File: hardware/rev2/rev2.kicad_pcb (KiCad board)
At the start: 4 copper layers, 60 x 40 mm, 1 part, among them U1 SX1262IMLTRT

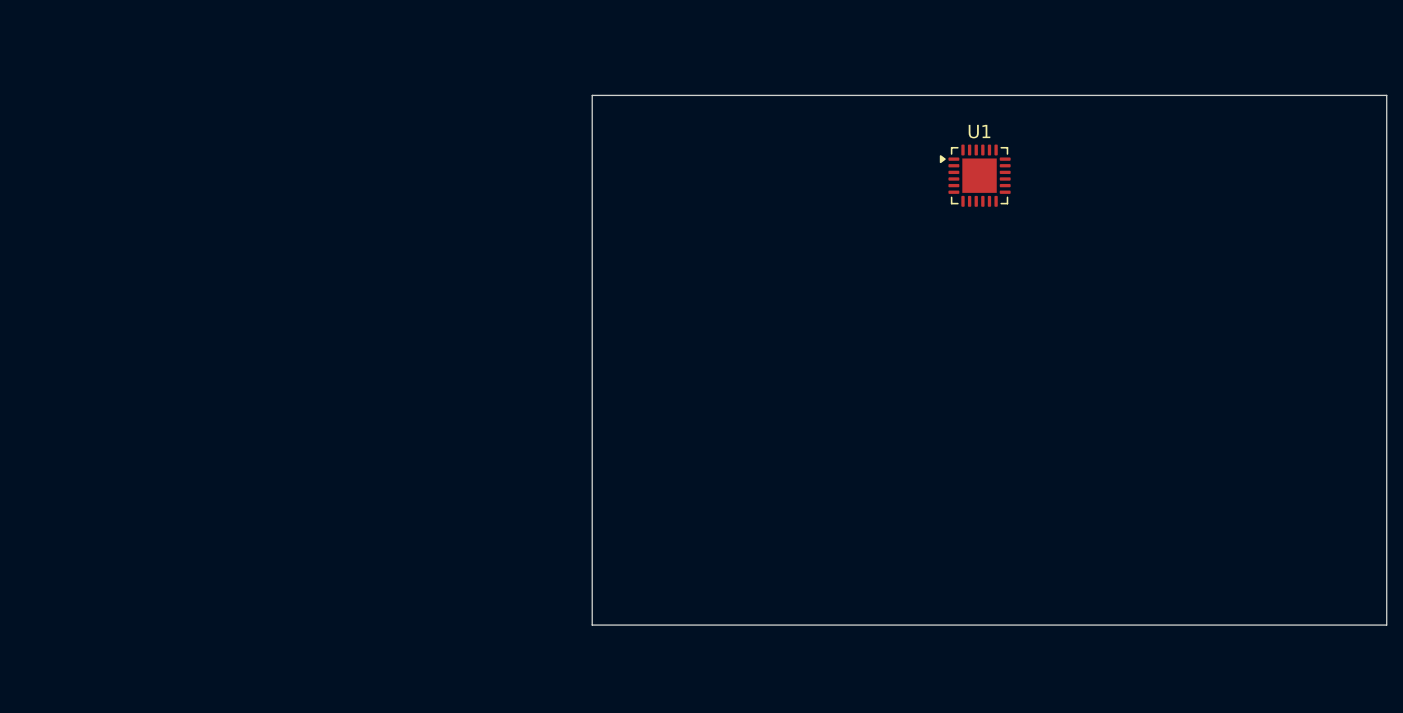
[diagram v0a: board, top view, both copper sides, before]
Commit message: fixed some ERC errors and warnings, added USB, assigned a bunch of footprints
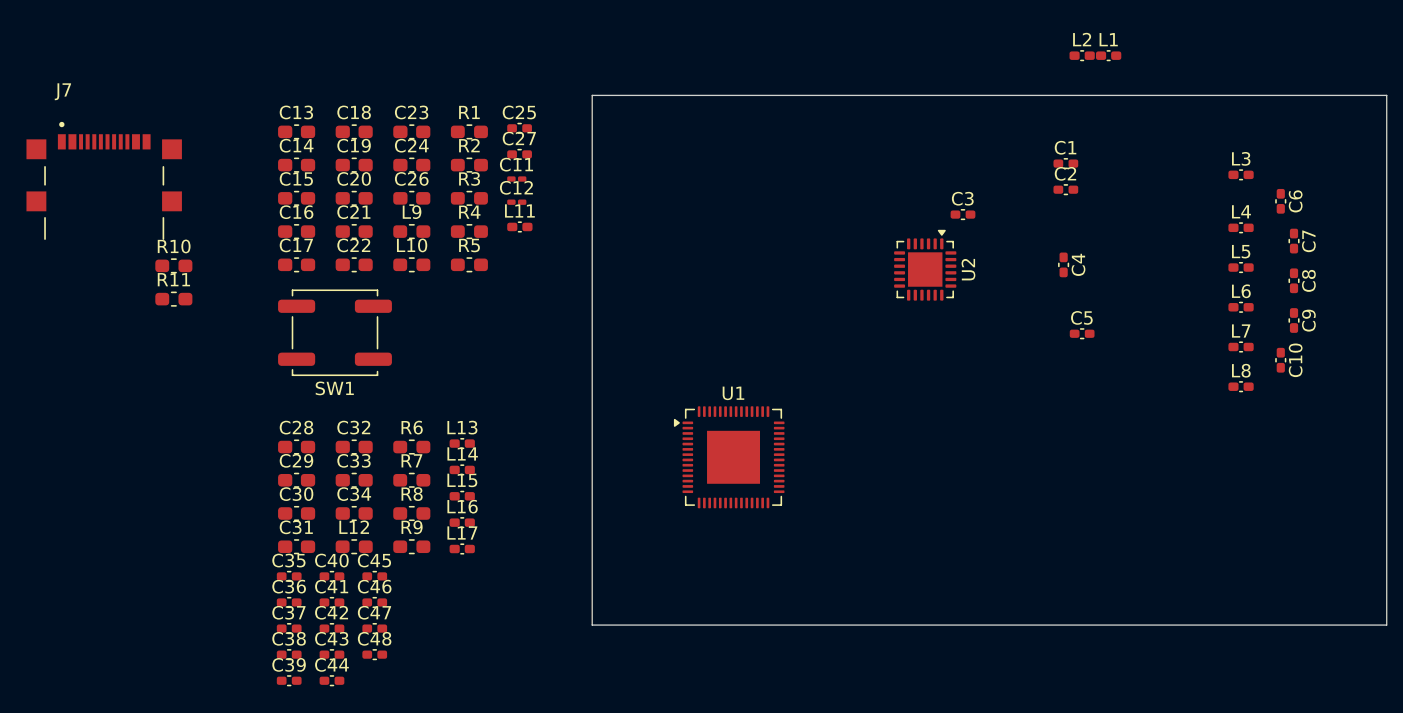
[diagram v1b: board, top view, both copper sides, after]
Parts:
- added C1: TBD, Capacitor_SMD:C_0402_1005Metric_Pad0.74x0.62mm_HandSolder, F.Cu at (163.8, 62.1)
- added C10: DC-Block, Capacitor_SMD:C_0402_1005Metric_Pad0.74x0.62mm_HandSolder, F.Cu at (180.0, 77.0)
- added C11: NC, Capacitor_SMD:C_0201_0603Metric_Pad0.64x0.40mm_HandSolder, F.Cu at (122.3, 63.3)
- added C12: NC, Capacitor_SMD:C_0201_0603Metric_Pad0.64x0.40mm_HandSolder, F.Cu at (122.3, 65.1)
- added C13: 10 uF, Capacitor_SMD:C_0603_1608Metric_Pad1.08x0.95mm_HandSolder, F.Cu at (105.7, 59.8)
- added C14: TBD, Capacitor_SMD:C_0603_1608Metric_Pad1.08x0.95mm_HandSolder, F.Cu at (105.7, 62.3)
- added C15: 1 uF, Capacitor_SMD:C_0603_1608Metric_Pad1.08x0.95mm_HandSolder, F.Cu at (105.7, 64.8)
- added C16: 0.1 uF, Capacitor_SMD:C_0603_1608Metric_Pad1.08x0.95mm_HandSolder, F.Cu at (105.7, 67.3)
- added C17: 1 uF, Capacitor_SMD:C_0603_1608Metric_Pad1.08x0.95mm_HandSolder, F.Cu at (105.7, 69.8)
- added C18: TBD, Capacitor_SMD:C_0603_1608Metric_Pad1.08x0.95mm_HandSolder, F.Cu at (110.0, 59.8)
- added C19: 0.1 uF, Capacitor_SMD:C_0603_1608Metric_Pad1.08x0.95mm_HandSolder, F.Cu at (110.0, 62.3)
- added C2: TBD, Capacitor_SMD:C_0402_1005Metric_Pad0.74x0.62mm_HandSolder, F.Cu at (163.8, 64.1)
- added C20: 0.1 uF, Capacitor_SMD:C_0603_1608Metric_Pad1.08x0.95mm_HandSolder, F.Cu at (110.0, 64.8)
- added C21: 10 nF, Capacitor_SMD:C_0603_1608Metric_Pad1.08x0.95mm_HandSolder, F.Cu at (110.0, 67.3)
- added C22: 0.1 uF, Capacitor_SMD:C_0603_1608Metric_Pad1.08x0.95mm_HandSolder, F.Cu at (110.0, 69.8)
- added C23: 0.1 uF, Capacitor_SMD:C_0603_1608Metric_Pad1.08x0.95mm_HandSolder, F.Cu at (114.4, 59.8)
- added C24: 1 uF, Capacitor_SMD:C_0603_1608Metric_Pad1.08x0.95mm_HandSolder, F.Cu at (114.4, 62.3)
- added C25: TBD, Capacitor_SMD:C_0402_1005Metric_Pad0.74x0.62mm_HandSolder, F.Cu at (122.5, 59.5)
- added C26: 1 uF, Capacitor_SMD:C_0603_1608Metric_Pad1.08x0.95mm_HandSolder, F.Cu at (114.4, 64.8)
- added C27: TBD, Capacitor_SMD:C_0402_1005Metric_Pad0.74x0.62mm_HandSolder, F.Cu at (122.5, 61.5)
- added C28: 100n, Capacitor_SMD:C_0603_1608Metric_Pad1.08x0.95mm_HandSolder, F.Cu at (105.7, 83.6)
- added C29: TBD, Capacitor_SMD:C_0603_1608Metric_Pad1.08x0.95mm_HandSolder, F.Cu at (105.7, 86.1)
- added C3: TBD, Capacitor_SMD:C_0402_1005Metric_Pad0.74x0.62mm_HandSolder, F.Cu at (156.0, 66.0)
- added C30: 10p, Capacitor_SMD:C_0603_1608Metric_Pad1.08x0.95mm_HandSolder, F.Cu at (105.7, 88.6)
- added C31: 100n, Capacitor_SMD:C_0603_1608Metric_Pad1.08x0.95mm_HandSolder, F.Cu at (105.7, 91.1)
- added C32: 100n, Capacitor_SMD:C_0603_1608Metric_Pad1.08x0.95mm_HandSolder, F.Cu at (110.0, 83.6)
- added C33: TBD, Capacitor_SMD:C_0603_1608Metric_Pad1.08x0.95mm_HandSolder, F.Cu at (110.0, 86.1)
- added C34: 470n, Capacitor_SMD:C_0603_1608Metric_Pad1.08x0.95mm_HandSolder, F.Cu at (110.0, 88.6)
- added C35: DC Block, Capacitor_SMD:C_0402_1005Metric_Pad0.74x0.62mm_HandSolder, F.Cu at (105.1, 93.3)
- added C36: C, Capacitor_SMD:C_0402_1005Metric_Pad0.74x0.62mm_HandSolder, F.Cu at (105.1, 95.3)
- added C37: 47p, Capacitor_SMD:C_0402_1005Metric_Pad0.74x0.62mm_HandSolder, F.Cu at (105.1, 97.3)
- added C38: 47n, Capacitor_SMD:C_0402_1005Metric_Pad0.74x0.62mm_HandSolder, F.Cu at (105.1, 99.2)
- added C39: C, Capacitor_SMD:C_0402_1005Metric_Pad0.74x0.62mm_HandSolder, F.Cu at (105.1, 101.2)
- added C4: TBD, Capacitor_SMD:C_0402_1005Metric_Pad0.74x0.62mm_HandSolder, F.Cu at (163.6, 69.8)
- added C40: C, Capacitor_SMD:C_0402_1005Metric_Pad0.74x0.62mm_HandSolder, F.Cu at (108.3, 93.3)
- added C41: C, Capacitor_SMD:C_0402_1005Metric_Pad0.74x0.62mm_HandSolder, F.Cu at (108.3, 95.3)
- added C42: DC Block, Capacitor_SMD:C_0402_1005Metric_Pad0.74x0.62mm_HandSolder, F.Cu at (108.3, 97.3)
- added C43: C, Capacitor_SMD:C_0402_1005Metric_Pad0.74x0.62mm_HandSolder, F.Cu at (108.3, 99.2)
- added C44: 1n, Capacitor_SMD:C_0402_1005Metric_Pad0.74x0.62mm_HandSolder, F.Cu at (108.3, 101.2)
- added C45: 1n, Capacitor_SMD:C_0402_1005Metric_Pad0.74x0.62mm_HandSolder, F.Cu at (111.6, 93.3)
- added C46: DC Block, Capacitor_SMD:C_0402_1005Metric_Pad0.74x0.62mm_HandSolder, F.Cu at (111.6, 95.3)
- added C47: C, Capacitor_SMD:C_0402_1005Metric_Pad0.74x0.62mm_HandSolder, F.Cu at (111.6, 97.3)
- added C48: C, Capacitor_SMD:C_0402_1005Metric_Pad0.74x0.62mm_HandSolder, F.Cu at (111.6, 99.2)
- added C5: DC-Block, Capacitor_SMD:C_0402_1005Metric_Pad0.74x0.62mm_HandSolder, F.Cu at (165.0, 75.0)
- added C6: DC-Block, Capacitor_SMD:C_0402_1005Metric_Pad0.74x0.62mm_HandSolder, F.Cu at (180.0, 65.0)
- added C7: DC-Block, Capacitor_SMD:C_0402_1005Metric_Pad0.74x0.62mm_HandSolder, F.Cu at (181.0, 68.0)
- added C8: DC-Block, Capacitor_SMD:C_0402_1005Metric_Pad0.74x0.62mm_HandSolder, F.Cu at (181.0, 71.0)
- added C9: DC-Block, Capacitor_SMD:C_0402_1005Metric_Pad0.74x0.62mm_HandSolder, F.Cu at (181.0, 74.0)
- added J7: USB_C_Receptacle_USB2.0_16P, _footprints:SAMESKY_UJ20-C-H-G-SMT-5-P16-TR, F.Cu at (91.1, 64.2)
- added L1: TBD, Inductor_SMD:L_0402_1005Metric_Pad0.77x0.64mm_HandSolder, F.Cu at (167.0, 54.0)
- added L10: 2.0 nH (0.1 nH), Inductor_SMD:L_0603_1608Metric_Pad1.05x0.95mm_HandSolder, F.Cu at (114.4, 69.8)
- added L11: TBD, Inductor_SMD:L_0402_1005Metric_Pad0.77x0.64mm_HandSolder, F.Cu at (122.5, 66.9)
- added L12: 15u, Inductor_SMD:L_0603_1608Metric_Pad1.05x0.95mm_HandSolder, F.Cu at (110.0, 91.1)
- added L13: L, Inductor_SMD:L_0402_1005Metric_Pad0.77x0.64mm_HandSolder, F.Cu at (118.2, 83.3)
- added L14: 115n, Inductor_SMD:L_0402_1005Metric_Pad0.77x0.64mm_HandSolder, F.Cu at (118.2, 85.3)
- added L15: L, Inductor_SMD:L_0402_1005Metric_Pad0.77x0.64mm_HandSolder, F.Cu at (118.2, 87.3)
- added L16: L, Inductor_SMD:L_0402_1005Metric_Pad0.77x0.64mm_HandSolder, F.Cu at (118.2, 89.3)
- added L17: L, Inductor_SMD:L_0402_1005Metric_Pad0.77x0.64mm_HandSolder, F.Cu at (118.2, 91.3)
- added L2: TBD, Inductor_SMD:L_0402_1005Metric_Pad0.77x0.64mm_HandSolder, F.Cu at (165.0, 54.0)
- added L3: Choke, Inductor_SMD:L_0402_1005Metric_Pad0.77x0.64mm_HandSolder, F.Cu at (177.0, 63.0)
- added L4: Choke, Inductor_SMD:L_0402_1005Metric_Pad0.77x0.64mm_HandSolder, F.Cu at (177.0, 67.0)
- added L5: Choke, Inductor_SMD:L_0402_1005Metric_Pad0.77x0.64mm_HandSolder, F.Cu at (177.0, 70.0)
- added L6: Choke, Inductor_SMD:L_0402_1005Metric_Pad0.77x0.64mm_HandSolder, F.Cu at (177.0, 73.0)
- added L7: Choke, Inductor_SMD:L_0402_1005Metric_Pad0.77x0.64mm_HandSolder, F.Cu at (177.0, 76.0)
- added L8: Choke, Inductor_SMD:L_0402_1005Metric_Pad0.77x0.64mm_HandSolder, F.Cu at (177.0, 79.0)
- added L9: TBD (24 nH), Inductor_SMD:L_0603_1608Metric_Pad1.05x0.95mm_HandSolder, F.Cu at (114.4, 67.3)
- added R1: 10K, Inductor_SMD:L_0603_1608Metric_Pad1.05x0.95mm_HandSolder, F.Cu at (118.7, 59.8)
- added R10: 5.1k, Inductor_SMD:L_0603_1608Metric_Pad1.05x0.95mm_HandSolder, F.Cu at (96.4, 69.9)
- added R11: 5.1k, Inductor_SMD:L_0603_1608Metric_Pad1.05x0.95mm_HandSolder, F.Cu at (96.4, 72.4)
- added R2: 22R, Inductor_SMD:L_0603_1608Metric_Pad1.05x0.95mm_HandSolder, F.Cu at (118.7, 62.3)
- added R3: 22R, Inductor_SMD:L_0603_1608Metric_Pad1.05x0.95mm_HandSolder, F.Cu at (118.7, 64.8)
- added R4: 10K, Inductor_SMD:L_0603_1608Metric_Pad1.05x0.95mm_HandSolder, F.Cu at (118.7, 67.3)
- added R5: 10K, Inductor_SMD:L_0603_1608Metric_Pad1.05x0.95mm_HandSolder, F.Cu at (118.7, 69.8)
- added R6: pull-up, Inductor_SMD:L_0603_1608Metric_Pad1.05x0.95mm_HandSolder, F.Cu at (114.4, 83.6)
- added R7: 220R, Inductor_SMD:L_0603_1608Metric_Pad1.05x0.95mm_HandSolder, F.Cu at (114.4, 86.1)
- added R8: 100R, Inductor_SMD:L_0603_1608Metric_Pad1.05x0.95mm_HandSolder, F.Cu at (114.4, 88.6)
- added R9: 100R, Inductor_SMD:L_0603_1608Metric_Pad1.05x0.95mm_HandSolder, F.Cu at (114.4, 91.1)
- added SW1: SW_Push, Button_Switch_SMD:SW_Push_1P1T_NO_CK_KSC7xxJ, F.Cu at (108.6, 74.9)
- added U1: ESP32-S3, Package_DFN_QFN:QFN-56-1EP_7x7mm_P0.4mm_EP4x4mm, F.Cu at (138.7, 84.3)
- moved U2 8.19 mm to (153.2, 70.2), turned to -90 degrees
- renumbered U1 to U2
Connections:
- U2 pad 13: /SX1262/DIO1 -> /ESP32/DIO1
- U2 pad 14: /SX1262/BUSY -> /ESP32/BUSY
- U2 pad 15: /SX1262/RESET -> /SX1262/Reset
- U2 pad 16: /SX1262/MISO -> /ESP32/MISO
- U2 pad 17: /SX1262/MOSI -> /ESP32/MOSI
- U2 pad 18: /SX1262/SCK -> /ESP32/SCK
- U2 pad 19: /SX1262/CS -> /ESP32/CS

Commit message: ESP32 approaching final schematic. tidied up a lot and changed GPIO pins.
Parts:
- L10: value 2.0 nH (0.1 nH) -> 2.0 nH 500mA
- U1: value ESP32-S3 -> ESP32-S3FN8
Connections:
- net /ESP32/XIN renamed Net-(C14-Pad1)
- net /ESP32/XOUT renamed Net-(U1-XTAL_N)
- C13 pad 1: /ESP32/VDD33 -> +3V3
- C15 pad 1: /ESP32/VDD33 -> +3V3
- C16 pad 1: /ESP32/VDD33 -> +3V3
- C17 pad 1: /ESP32/VDD33 -> +3V3
- C19 pad 1: /ESP32/VDD33 -> +3V3
- C21 pad 1: /ESP32/VDD33 -> +3V3
- C22 pad 1: /ESP32/VDD_SPI -> +3V3
- C23 pad 1: /ESP32/VDD33 -> +3V3
- C24 pad 1: /ESP32/VDD_SPI -> +3V3
- L10 pad 1: /ESP32/VDD33 -> +3V3
- R1 pad 1: /ESP32/VDD33 -> +3V3
- R2 pad 2: Net-(U1-GPIO19/USB_D-) -> unconnected-(R2-Pad2)
- R3 pad 1: /USB_D+ -> unconnected-(R3-Pad1)
- R3 pad 2: Net-(U1-GPIO20/USB_D+) -> /USB_D+
- R4 pad 1: +3V3 -> GND
- U1 pad 20: /ESP32/VDD33 -> +3V3
- U1 pad 25: Net-(U1-GPIO19/USB_D-) -> /USB_D-
- U1 pad 26: Net-(U1-GPIO20/USB_D+) -> /USB_D+
- U1 pad 29: /ESP32/VDD_SPI -> +3V3
- U1 pad 46: /ESP32/VDD33 -> +3V3
- U1 pad 55: /ESP32/VDD33 -> +3V3
- U1 pad 56: /ESP32/VDD33 -> +3V3
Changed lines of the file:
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@@
 			(layers "F.Cu" "F.Mask" "F.Paste")
 			(roundrect_rratio 0.25)
-			(net "/ESP32/XIN")
+			(net "Net-(C14-Pad1)")
 			(pintype "passive")
 		)
@@
 			(layers "F.Cu" "F.Mask" "F.Paste")
 			(roundrect_rratio 0.25)
-			(net "/ESP32/VDD33")
+			(net "+3V3")
 			(pintype "passive")
 		)
@@
 			(layers "F.Cu" "F.Mask" "F.Paste")
 			(roundrect_rratio 0.25)
-			(net "Net-(U1-GPIO19{slash}USB_D-)")
+			(net "unconnected-(R2-Pad2)")
 			(pintype "passive")
 		)
@@
 			(layers "F.Cu" "F.Mask" "F.Paste")
 			(roundrect_rratio 0.25)
-			(net "/ESP32/VDD_SPI")
+			(net "+3V3")
 			(pintype "passive")
 		)
@@
 			(layers "F.Cu" "F.Mask" "F.Paste")
 			(roundrect_rratio 0.25)
-			(net "/ESP32/VDD33")
+			(net "+3V3")
 			(pintype "passive")
 		)
@@
 			(layers "F.Cu" "F.Mask" "F.Paste")
 			(roundrect_rratio 0.25)
-			(net "/ESP32/XOUT")
+			(net "Net-(U1-XTAL_N)")
 			(pintype "passive")
 		)
@@
 			)
 		)
-		(property "Value" "ESP32-S3"
+		(property "Value" "ESP32-S3FN8"
 			(at 0 4.8 0)
 			(layer "F.Fab")
@@
 			(layers "F.Cu" "F.Mask" "F.Paste")
 			(roundrect_rratio 0.25)
-			(net "/ESP32/VDD33")
+			(net "+3V3")
 			(pinfunction "VDD3P3_RTC_20")
 			(pintype "power_in")
@@
 			(layers "F.Cu" "F.Mask" "F.Paste")
 			(roundrect_rratio 0.25)
-			(net "Net-(U1-GPIO19{slash}USB_D-)")
+			(net "/USB_D-")
 			(pinfunction "GPIO19/USB_D-_25")
 			(pintype "bidirectional")
@@
 			(layers "F.Cu" "F.Mask" "F.Paste")
 			(roundrect_rratio 0.25)
-			(net "Net-(U1-GPIO20{slash}USB_D+)")
+			(net "/USB_D+")
 			(pinfunction "GPIO20/USB_D+_26")
 			(pintype "bidirectional")
@@
 			(layers "F.Cu" "F.Mask" "F.Paste")
 			(roundrect_rratio 0.25)
-			(net "/ESP32/VDD_SPI")
+			(net "+3V3")
 			(pinfunction "VDD_SPI_29")
 			(pintype "power_in")
@@
 			(layers "F.Cu" "F.Mask" "F.Paste")
 			(roundrect_rratio 0.25)
-			(net "/ESP32/VDD33")
+			(net "+3V3")
 			(pinfunction "VDD3P3_CPU_46")
 			(pintype "power_in")
@@
 			(layers "F.Cu" "F.Mask" "F.Paste")
 			(roundrect_rratio 0.25)
-			(net "/ESP32/XOUT")
+			(net "Net-(U1-XTAL_N)")
 			(pinfunction "XTAL_N_53")
 			(pintype "output")
@@
 			(layers "F.Cu" "F.Mask" "F.Paste")
 			(roundrect_rratio 0.25)
-			(net "/ESP32/VDD33")
+			(net "+3V3")
 			(pinfunction "VDDA_55")
 			(pintype "power_in")
@@
 			(layers "F.Cu" "F.Mask" "F.Paste")
 			(roundrect_rratio 0.25)
-			(net "/ESP32/VDD33")
+			(net "+3V3")
 			(pinfunction "VDDA_56")
 			(pintype "passive")
@@
 			(layers "F.Cu" "F.Mask" "F.Paste")
 			(roundrect_rratio 0.25)
-			(net "/ESP32/VDD33")
+			(net "+3V3")
 			(pintype "passive")
 		)
@@
 			(layers "F.Cu" "F.Mask" "F.Paste")
 			(roundrect_rratio 0.25)
-			(net "/ESP32/VDD33")
+			(net "+3V3")
 			(pintype "passive")
 		)
@@
 			(layers "F.Cu" "F.Mask" "F.Paste")
 			(roundrect_rratio 0.25)
-			(net "/ESP32/VDD33")
+			(net "+3V3")
 			(pintype "passive")
 		)
@@
 			)
 		)
-		(property "Value" "2.0 nH (0.1 nH)"
+		(property "Value" "2.0 nH 500mA"
 			(at 0 1.43 0)
 			(layer "F.Fab")
@@
 			(layers "F.Cu" "F.Mask" "F.Paste")
 			(roundrect_rratio 0.25)
-			(net "/ESP32/VDD33")
+			(net "+3V3")
 			(pinfunction "1_1")
 			(pintype "passive")
@@
 			(layers "F.Cu" "F.Mask" "F.Paste")
 			(roundrect_rratio 0.25)
-			(net "/ESP32/VDD33")
+			(net "+3V3")
 			(pintype "passive")
 		)
@@
 			(layers "F.Cu" "F.Mask" "F.Paste")
 			(roundrect_rratio 0.25)
-			(net "/ESP32/VDD33")
+			(net "+3V3")
 			(pintype "passive")
 		)
@@
 			(layers "F.Cu" "F.Mask" "F.Paste")
 			(roundrect_rratio 0.25)
-			(net "/USB_D+")
+			(net "unconnected-(R3-Pad1)")
 			(pintype "passive")
 		)
@@
 			(layers "F.Cu" "F.Mask" "F.Paste")
 			(roundrect_rratio 0.25)
-			(net "Net-(U1-GPIO20{slash}USB_D+)")
+			(net "/USB_D+")
 			(pintype "passive")
 		)
@@
 			(layers "F.Cu" "F.Mask" "F.Paste")
 			(roundrect_rratio 0.25)
-			(net "/ESP32/XIN")
+			(net "Net-(C14-Pad1)")
 			(pinfunction "1_1")
 			(pintype "passive")
@@
 			(layers "F.Cu" "F.Mask" "F.Paste")
 			(roundrect_rratio 0.25)
-			(net "/ESP32/VDD33")
+			(net "+3V3")
 			(pintype "passive")
 		)
@@
 			)
 		)
-		(attr smd exclude_from_bom dnp)
+		(attr smd exclude_from_bom)
 		(duplicate_pad_numbers_are_jumpers no)
 		(fp_line
@@
 			(layers "F.Cu" "F.Mask" "F.Paste")
 			(roundrect_rratio 0.25)
-			(net "+3V3")
+			(net "GND")
 			(pintype "passive")
 		)
@@
 			(layers "F.Cu" "F.Mask" "F.Paste")
 			(roundrect_rratio 0.25)
-			(net "/ESP32/VDD_SPI")
+			(net "+3V3")
 			(pintype "passive")
 		)
